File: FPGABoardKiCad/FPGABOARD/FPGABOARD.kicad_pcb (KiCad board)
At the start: 4 copper layers, 78 x 51 mm, 80 parts, among them J1 USB_C_Receptacle_USB2.0_14P, J3 12PMOD, J4 6PMOD, J5 I2C, J6 Conn_02x13_Odd_Even, SW1 ResetICE, SW2 BTN0, SW3 BTN1, SW4 BTN2, U1 AP2127K-1.2, U2 AP2127K-3.3, U3 W25Q32JVSS, U4 93LCxxBxxOT, U5 FT2232HPQ, U6 IS62LV256AL, U7 ICE40HX1K-VQ100, Y1 SG-210STF, Y2 SG-210STF

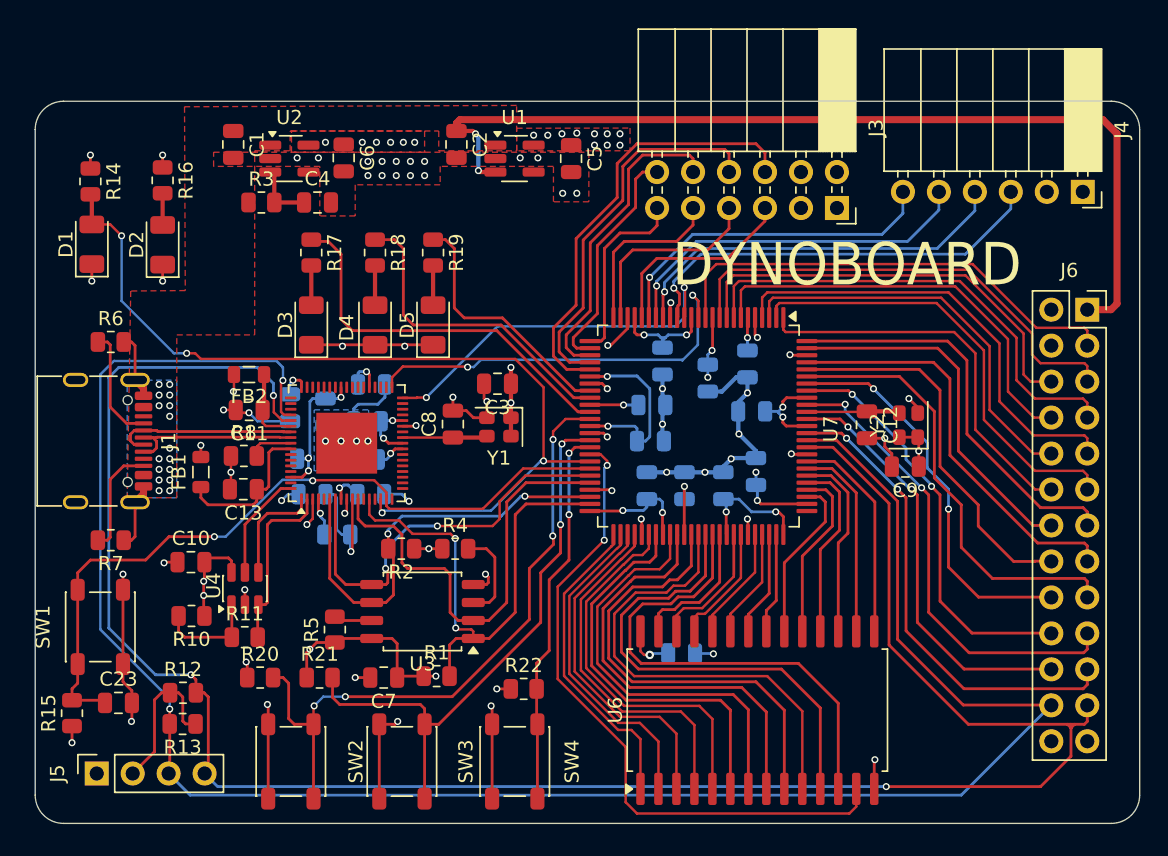
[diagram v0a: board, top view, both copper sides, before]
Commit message: Add programing header
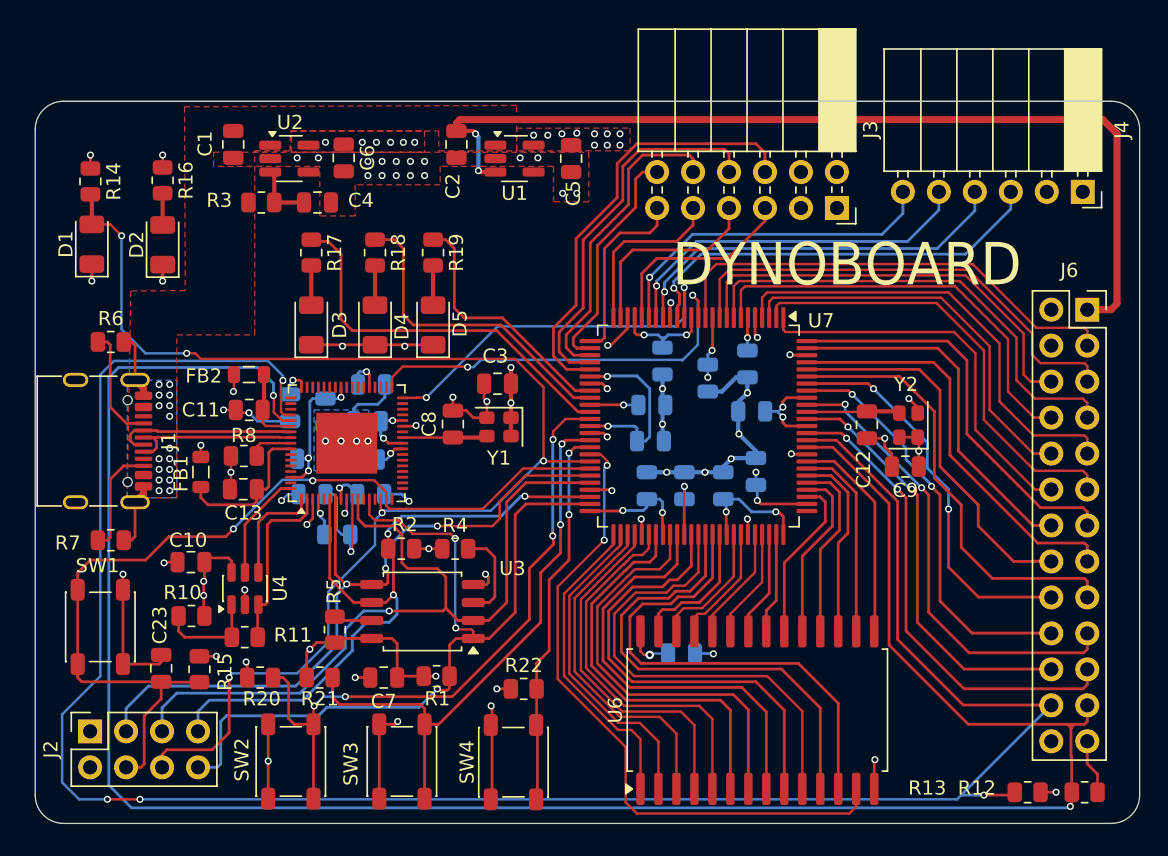
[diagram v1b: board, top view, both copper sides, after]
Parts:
- removed J5: I2C, Connector_PinSocket_2.54mm:PinSocket_1x04_P2.54mm_Vertical
- added J2: Program, Connector_PinSocket_2.54mm:PinSocket_2x04_P2.54mm_Vertical, F.Cu at (83.9, 120.5)
- moved R12 64.1 mm to (154.1, 124.8), turned to 180 degrees
- moved R13 59.9 mm to (150.1, 124.8)
- moved R15 9.52 mm to (91.6, 116.1), turned to -90 degrees
- moved C23 3.88 mm to (88.9, 116.0), turned to 90 degrees
- moved SW4 0.11 mm to (113.8, 122.7)
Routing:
- net /CDONE: track 63.9 -> 94.1 mm, vias 4 -> 5
- net /ICE_SDI: track 31.7 -> 56.8 mm, vias 0 -> 1
- net /ICE_SDO: track 29.1 -> 52.0 mm, vias 2 -> 3
- net /ICE_SS: track 37.1 -> 59.9 mm, vias 2 -> 3
- net /ICE_SCK: track 31.0 -> 51.4 mm, vias 2 -> 3
- net /CRESET_B: track 53.4 -> 65.4 mm
- net /SCL: track 144.0 -> 154.7 mm, vias 2 -> 4
- net +3V3: track 117.0 -> 111.2 mm, vias 38 -> 39
- net /SDA: track 149.1 -> 154.9 mm, vias 3 -> 2
- net GND: track 126.3 -> 123.8 mm, vias 64 -> 63

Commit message: Changed to 0603
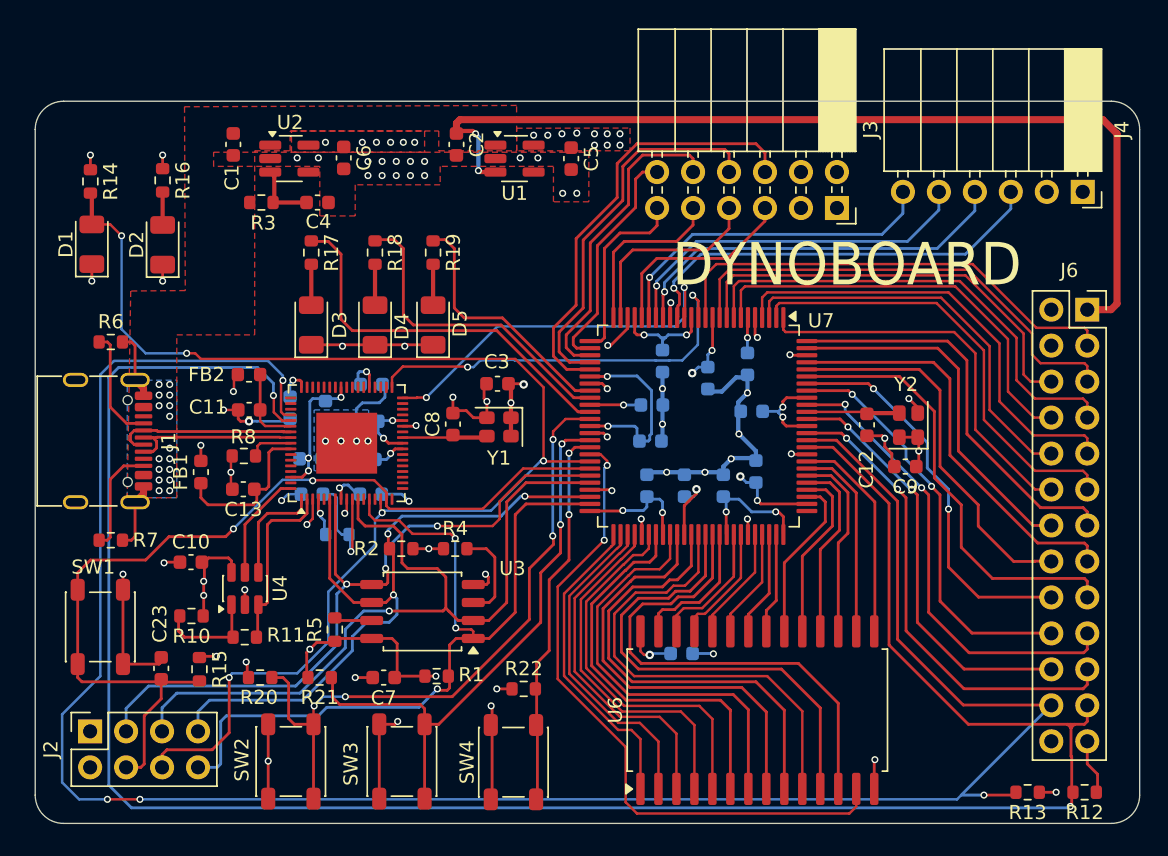
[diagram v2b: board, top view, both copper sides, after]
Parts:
- C1, C10, C11, C12, C13, C14, C15, C16, C17, C18, C19, C2, C20, C21, C22, C23, C24, C25, C26, C27, C28, C29, C3, C30, C31, C32, C34, C4, C5, C6, C7, C8, C9: footprint Capacitor_SMD:C_0805_2012Metric -> Capacitor_SMD:C_0603_1608Metric
- FB1, FB2: footprint Inductor_SMD:L_0805_2012Metric -> Inductor_SMD:L_0603_1608Metric
- R1, R10, R11, R12, R13, R14, R15, R16, R17, R18, R19, R2, R20, R21, R22, R3, R4, R5, R6, R7, R8, R9: footprint Resistor_SMD:R_0805_2012Metric -> Resistor_SMD:R_0603_1608Metric
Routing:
- net +1V2: track 32.5 -> 33.7 mm

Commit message: Images
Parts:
- moved R12 0.14 mm to (154.0, 124.8)
